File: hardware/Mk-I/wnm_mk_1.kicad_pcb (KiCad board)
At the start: 2 copper layers, 96.5 x 67.1 mm, 126 parts, among them CON1 USB-MICRO-B, SW1 SW_PUSH, SW10 SW_PUSH, SW11 SW_PUSH, SW12 SW_PUSH, SW13 SW_PUSH, SW14 SW_PUSH, SW15 SW_PUSH, SW16 SW_PUSH, SW18 SW_PUSH, SW19 SW_PUSH, SW2 SW_PUSH, SW20 SW_PUSH, SW21 SW_PUSH, SW22 SW_PUSH, SW3 SW_PUSH, SW4 SW_PUSH, SW5 SW_PUSH, SW6 SW_PUSH, SW7 SW_PUSH, SW8 SW_PUSH, SW9 SW_PUSH, U1 AP7313-18-SR-G-7, U10 STM32_SWD_Connector, U2 MCP73831, U3 BD33IA5, U4 STM32F407VG, U5 SGTL5000, U6 encoder_and_switch, U7 encoder_and_switch, U8 MOLEX_microSD_47219-2001, U9 SSD1306, X1 CRYSTAL

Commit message: HW: Update parts value
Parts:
- BAT1, D1, D10, D11, D12, D13, D14, D15, D16, D17, D2, D25, D3, D4, D5, D6, D7, D8, D9: value LED -> 150060RS75000
- CON1: value USB-MICRO-B -> 10118194-0001LF
- D18, D20, D21, D22, D23, D24: value LED -> 150060GS75000
- D27: value DOUBLE_SCH_KCOM_PMEG2005CT -> PMEG2005CT
- HP_OUT1, LINE_IN1: value 3.5_audio_jack -> lumberg 1503 02
- Play1, Play2, SW1, SW10, SW11, SW12, SW13, SW14, SW15, SW16, SW18, SW19, SW2, SW20, SW21, SW22, SW3, SW4, SW5, SW6, SW7, SW8, SW9, Write1: value SW_PUSH -> EVQ-Q2S02W
- U1: value AP7313-18-SR-G-7 -> AP7313-18SRG-7
- U2: value MCP73831 -> MCP73831T-2ACI/OT
- U3: value BD33IA5 -> BD33IA5MEFJ-ME2
- U4: value STM32F407VG -> STM32F427VIT6
- U5: value SGTL5000 -> SGTL5000XNAA3R2
- U6, U7: value encoder_and_switch -> EC12D1524403
- U8: value MOLEX_microSD_47219-2001 -> 47219-2001
- X1: value CRYSTAL -> AS-8.000-18

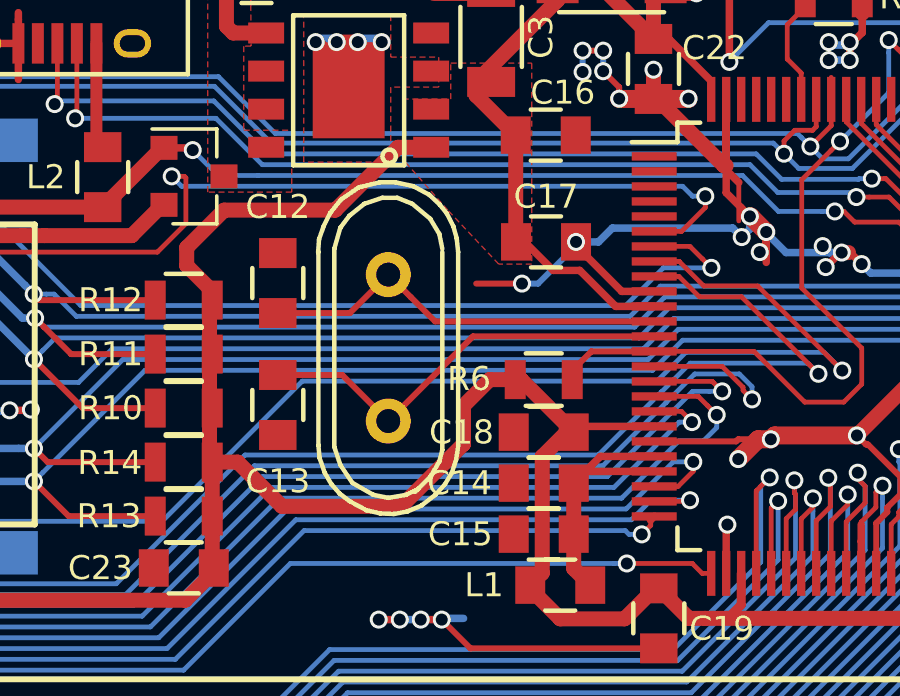
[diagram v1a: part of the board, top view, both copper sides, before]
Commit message: HW: Change crystal for a smd package
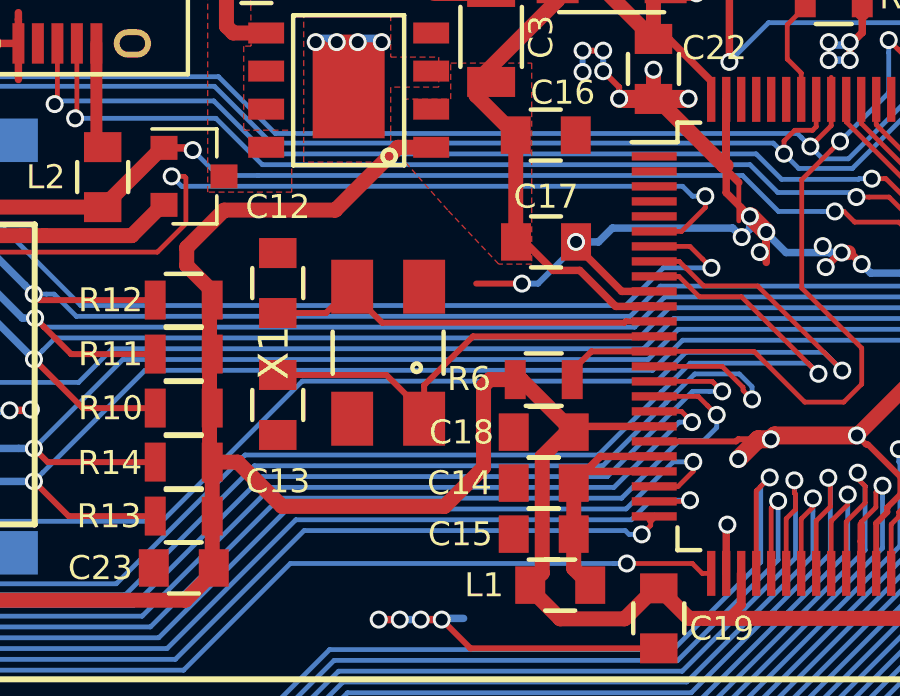
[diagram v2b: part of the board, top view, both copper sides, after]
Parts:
- HP_OUT1, LINE_IN1: value lumberg 1503 02 -> 1503 02
- X1: value AS-8.000-18 -> ABM3B-8.000MHZ-B2-T; footprint Crystals:Crystal_HC49-U_Vertical -> Crystals:Crystal_SMD_0603_4Pads
- moved X1 0.16 mm to (139.3, 93.3), turned to 90 degrees
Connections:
- X1 pad 1: Net-(C12-Pad2) -> Net-(C13-Pad2)
- X1 pad 2: Net-(C13-Pad2) -> GND
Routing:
- net 3V3: track 240.4 -> 241.2 mm
- net Net-(C13-Pad2): track 14.4 -> 15.1 mm

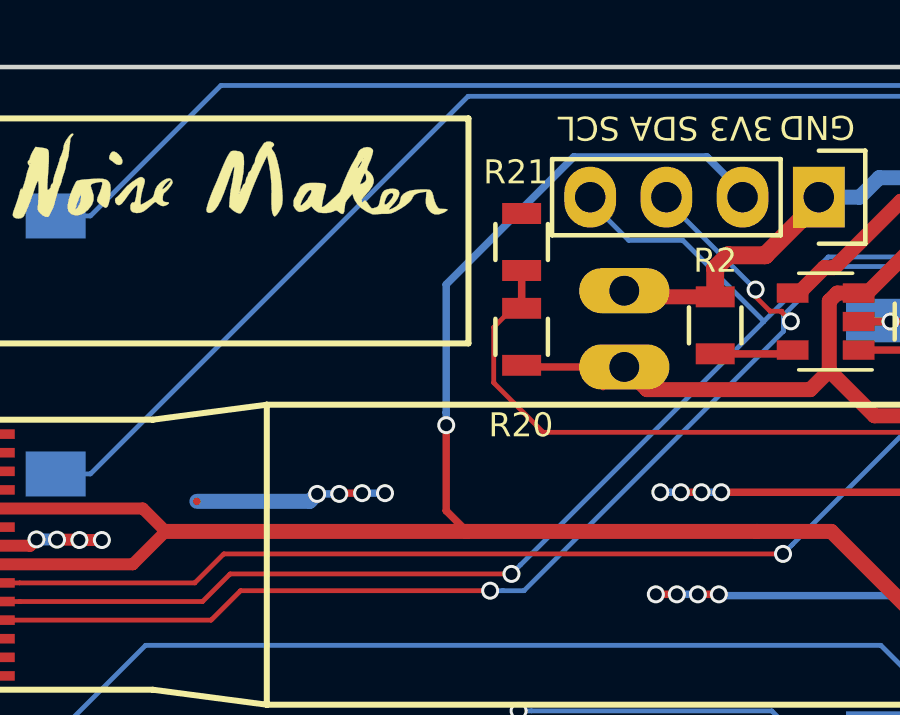
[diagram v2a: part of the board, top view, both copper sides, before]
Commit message: HW: Change battery connector to SMD
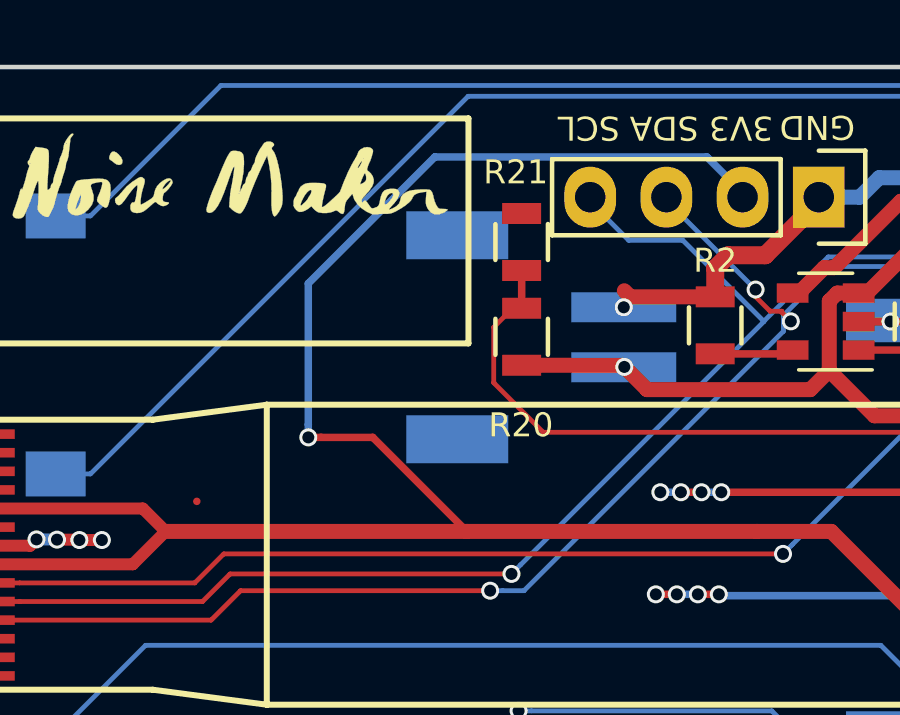
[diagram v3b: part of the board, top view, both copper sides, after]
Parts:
- BT1: value BATTERY -> S2B-PH-SM4-TB; footprint Connect:PINHEAD1-2 -> Connectors_JST:JST_PH_S2B-PH-SM4-TB_02x2.00mm_Angled
- moved BT1 2.81 mm to (107.2, 86.7)
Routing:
- net 3V3: track 241.2 -> 249.0 mm
- net (no net): track 6.39 -> 0.00 mm, vias 4 -> 0
- net VBAT: track 34.8 -> 33.8 mm, vias 0 -> 1
- net GND: track 217.0 -> 216.2 mm, vias 86 -> 87

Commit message: HW: Major change of layout...
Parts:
- removed D20, D21, D22, D23, D24: 150060GS75000, LEDs:LED_0805
- removed D25: 150060RS75000, LEDs:LED_0805
- removed REF**: MountingHole_4.3mm_M4, Mounting_Holes:MountingHole_4.3mm_M4
- removed SW18, SW19: EVQ-Q2S02W, Buttons_Switches_SMD:SW_SPST_B3SL-1002P
- removed ext1: CONN_01X04, Socket_Strips:Socket_Strip_Straight_1x04
- R9: value 330 -> 10K
- moved SW21 72.0 mm to (77.5, 123.2)
- moved SW20 65.1 mm to (77.5, 134.6)
- moved U9 29.4 mm to (111.8, 114.8)
- moved C25 29.3 mm to (109.0, 109.7)
- moved C27 29.3 mm to (109.0, 115.0)
- moved C28 29.3 mm to (109.0, 105.9)
- moved R15 29.3 mm to (109.0, 111.5)
- moved C29 29.3 mm to (109.0, 107.9)
- moved C26 29.3 mm to (109.0, 113.2)
- moved R9 24.3 mm to (182.2, 119.5), turned to 0 degrees
- moved LINE_IN1 10.6 mm to (72.0, 94.2)
- moved U6 10.2 mm to (78.7, 109.0)
- moved C30 10.2 mm to (74.1, 100.3)
- moved C31 10.2 mm to (83.3, 100.3)
- moved C32 10.2 mm to (90.2, 100.3)
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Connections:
- Play1 pad 1: Play -> 3V3
- Play1 pad 2: WAKEUP -> Play_WKUP
- Play2 pad 1: FX -> BUTTON_COL11
- Play2 pad 2: WAKEUP -> BUTTON_ROW2
- R9 pad 1: ROW3 -> GND
- R9 pad 2: Net-(D20-Pad2) -> Play_WKUP
- SW1 pad 1: B1 -> BUTTON_COL2
- SW1 pad 2: WAKEUP -> BUTTON_ROW1
- SW10 pad 1: B10 -> BUTTON_COL3
- SW10 pad 2: WAKEUP -> BUTTON_ROW2
- SW11 pad 1: B11 -> BUTTON_COL4
- SW11 pad 2: WAKEUP -> BUTTON_ROW2
- SW12 pad 1: B12 -> BUTTON_COL5
- SW12 pad 2: WAKEUP -> BUTTON_ROW2
- SW13 pad 1: B13 -> BUTTON_COL6
- SW13 pad 2: WAKEUP -> BUTTON_ROW2
- SW14 pad 1: B14 -> BUTTON_COL7
- SW14 pad 2: WAKEUP -> BUTTON_ROW2
- SW15 pad 1: B15 -> BUTTON_COL8
- SW15 pad 2: WAKEUP -> BUTTON_ROW2
- SW16 pad 1: B16 -> BUTTON_COL9
- SW16 pad 2: WAKEUP -> BUTTON_ROW2
- SW2 pad 1: B2 -> BUTTON_COL3
- SW2 pad 2: WAKEUP -> BUTTON_ROW1
- SW20 pad 1: BC -> BUTTON_COL1
- SW20 pad 2: WAKEUP -> BUTTON_ROW2
- SW21 pad 1: BD -> BUTTON_COL1
- SW21 pad 2: WAKEUP -> BUTTON_ROW1
- SW22 pad 1: BE -> BUTTON_COL10
- SW22 pad 2: WAKEUP -> BUTTON_ROW1
- SW3 pad 1: B3 -> BUTTON_COL4
- SW3 pad 2: WAKEUP -> BUTTON_ROW1
- SW4 pad 1: B4 -> BUTTON_COL5
- SW4 pad 2: WAKEUP -> BUTTON_ROW1
- SW5 pad 1: B5 -> BUTTON_COL6
- SW5 pad 2: WAKEUP -> BUTTON_ROW1
- SW6 pad 1: B6 -> BUTTON_COL7
- SW6 pad 2: WAKEUP -> BUTTON_ROW1
- SW7 pad 1: B7 -> BUTTON_COL8
- SW7 pad 2: WAKEUP -> BUTTON_ROW1
- SW8 pad 1: B8 -> BUTTON_COL9
- SW8 pad 2: WAKEUP -> BUTTON_ROW1
- SW9 pad 1: B9 -> BUTTON_COL2
- SW9 pad 2: WAKEUP -> BUTTON_ROW2
- U4 pad 16: B1 -> Net-(U4-Pad16)
- U4 pad 18: B9 -> Net-(U4-Pad18)
- U4 pad 23: WAKEUP -> PLAY_WAKEUP
- U4 pad 25: B2 -> Net-(U4-Pad25)
- U4 pad 33: B3 -> Net-(U4-Pad33)
- U4 pad 34: B11 -> Net-(U4-Pad34)
- U4 pad 36: BA -> Net-(U4-Pad36)
- U4 pad 38: B4 -> Net-(U4-Pad38)
- U4 pad 39: B12 -> Net-(U4-Pad39)
- U4 pad 41: BB -> Net-(U4-Pad41)
- U4 pad 42: B5 -> Net-(U4-Pad42)
- U4 pad 43: B13 -> Net-(U4-Pad43)
- U4 pad 45: BC -> Net-(U4-Pad45)
- U4 pad 46: B6 -> Net-(U4-Pad46)
- U4 pad 47: B14 -> Net-(U4-Pad47)
- U4 pad 51: B15 -> Net-(U4-Pad51)
- U4 pad 52: B7 -> Net-(U4-Pad52)
- U4 pad 53: BD -> Net-(U4-Pad53)
- U4 pad 55: BE -> Net-(U4-Pad55)
- U4 pad 56: B8 -> Net-(U4-Pad56)
- U4 pad 57: B16 -> Net-(U4-Pad57)
- U4 pad 58: ROW3 -> Net-(U4-Pad58)
- U4 pad 62: FX -> Net-(U4-Pad62)
- U4 pad 63: Play -> Net-(U4-Pad63)
- U6 pad 4: WAKEUP -> BUTTON_COL1
- U6 pad 5: ENC_1_SW -> BUTTON_ROW3
- U7 pad 4: WAKEUP -> BUTTON_COL3
- U7 pad 5: ENC_2_SW -> BUTTON_ROW3
- Write1 pad 1: Write -> BUTTON_COL10
- Write1 pad 2: WAKEUP -> BUTTON_ROW2
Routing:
- net WAKEUP: track 348.3 -> 0.00 mm, vias 1 -> 0
- net BUTTON_ROW2: track 0.00 -> 129.8 mm, vias 0 -> 2
- net BUTTON_ROW1: track 0.00 -> 104.2 mm, vias 0 -> 2
- net B9: track 101.4 -> 0.00 mm, vias 2 -> 0
- net B1: track 93.1 -> 0.00 mm, vias 2 -> 0
- net B10: track 86.3 -> 0.00 mm, vias 2 -> 0
- net COL1: track 98.4 -> 14.0 mm, vias 3 -> 2
- net B11: track 82.3 -> 0.00 mm, vias 2 -> 0
- net B12: track 80.9 -> 0.00 mm, vias 2 -> 0
- net ENC_1_SW: track 78.9 -> 0.00 mm, vias 1 -> 0
- net COL2: track 92.3 -> 14.2 mm, vias 3 -> 2
- net B2: track 75.5 -> 0.00 mm, vias 2 -> 0
- net B3: track 72.2 -> 0.00 mm, vias 2 -> 0
- net B13: track 70.8 -> 0.00 mm, vias 2 -> 0
- net ENC_1_A: track 79.9 -> 9.21 mm, vias 2 -> 1
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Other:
- board size 96.5 x 67.1 mm -> 106.7 x 67.1 mm
- board text added: "MENU"
- board text added: "PATTERN"
- board text added: "SHIFT"
- board text added: "TRACK"
- board text removed: "3V3"
- board text removed: "A"
- board text removed: "B"
- board text removed: "C"
- board text removed: "D"
- board text removed: "E"
- board text removed: "FX"
- board text removed: "SCL"
- board text removed: "SDA"

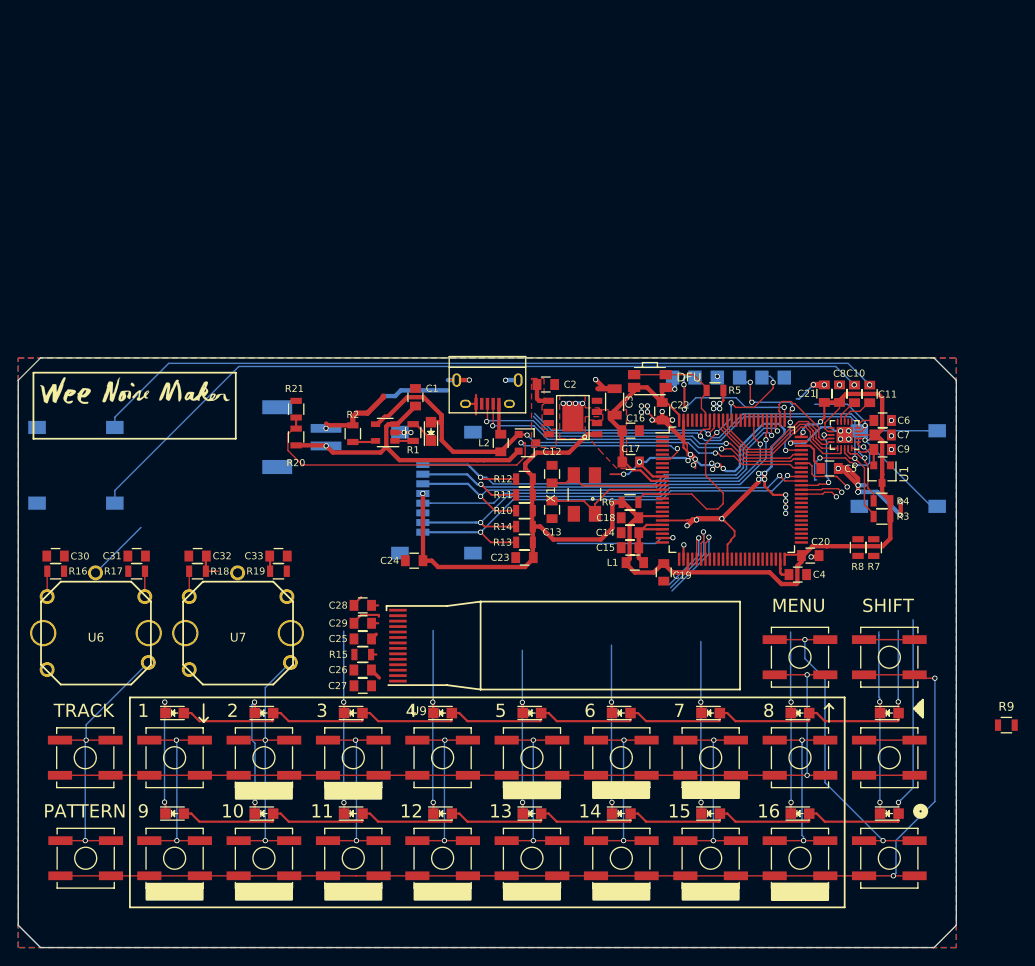
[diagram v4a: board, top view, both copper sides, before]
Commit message: HW: Change micro SD card slot
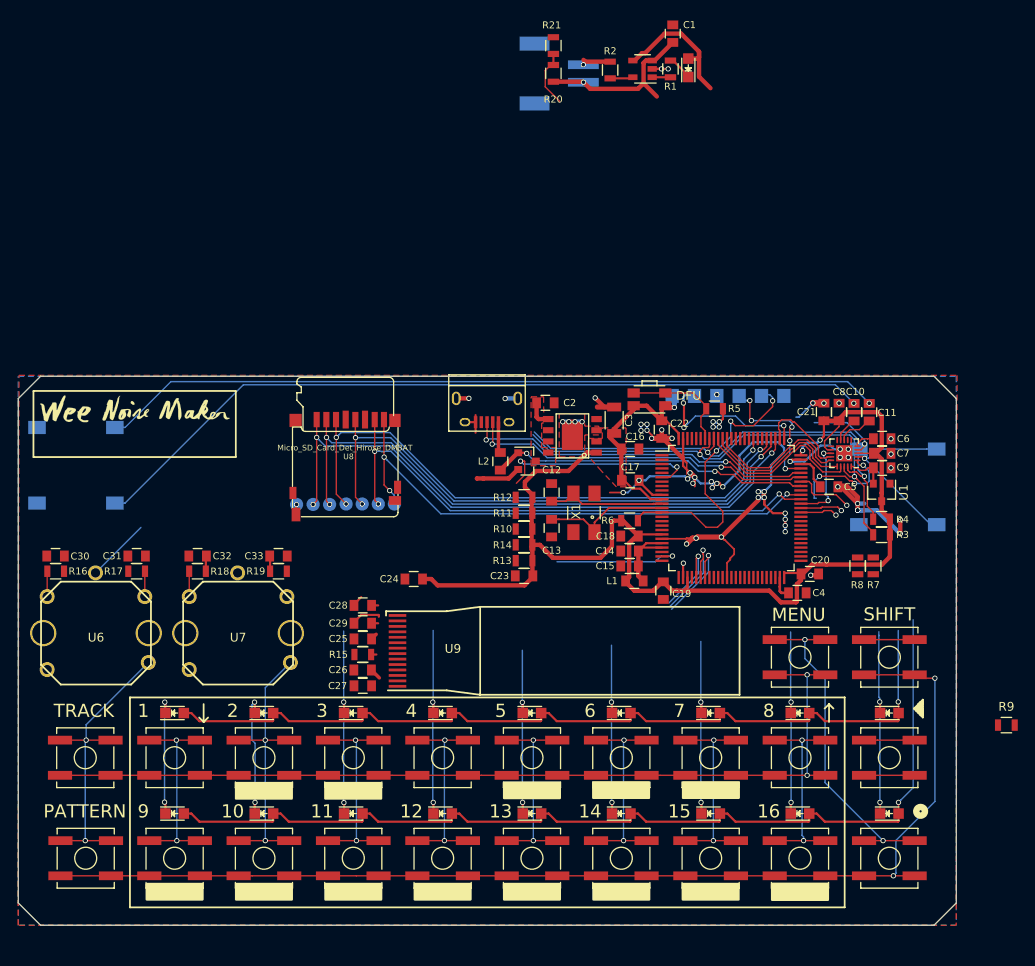
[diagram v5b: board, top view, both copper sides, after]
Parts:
- added TP_CLK1: TEST, Measurement_Points:Measurement_Point_Round-SMD-Pad_Small, B.Cu at (109.0, 94.3)
- added TP_CMD1: TEST, Measurement_Points:Measurement_Point_Round-SMD-Pad_Small, B.Cu at (107.1, 94.3)
- added TP_DAT0: TEST, Measurement_Points:Measurement_Point_Round-SMD-Pad_Small, B.Cu at (110.8, 94.3)
- added TP_DAT1: TEST, Measurement_Points:Measurement_Point_Round-SMD-Pad_Small, B.Cu at (112.6, 94.3)
- added TP_DAT2: TEST, Measurement_Points:Measurement_Point_Round-SMD-Pad_Small, B.Cu at (103.4, 94.4)
- added TP_DAT3: TEST, Measurement_Points:Measurement_Point_Round-SMD-Pad_Small, B.Cu at (105.3, 94.4)
- added TP_DETECT0: TEST, Measurement_Points:Measurement_Point_Round-SMD-Pad_Small, B.Cu at (101.5, 94.4)
- U8: value 47219-2001 -> Micro_SD_Card_Det_Hirose_DM3AT; footprint POSS:MOLEX_microSD_47219-2001 -> POSS:DM3D; moved to F.Cu
- moved BAT1 50.7 mm to (146.1, 44.7)
- moved R21 50.7 mm to (130.7, 42.2)
- moved C1 50.7 mm to (144.3, 40.8)
- moved R1 50.7 mm to (144.0, 44.9)
- moved R20 50.7 mm to (130.7, 45.4)
- moved BT1 50.7 mm to (131.3, 45.4)
- moved R2 50.7 mm to (137.2, 45.0)
- moved U2 50.7 mm to (140.8, 44.9)
- moved U8 15.6 mm to (113.0, 84.3), turned to 180 degrees
- moved C13 2.08 mm to (130.5, 97.1)
- moved C14 2.08 mm to (139.4, 99.7)
- moved C16 2.08 mm to (139.4, 88.1)
- moved C4 2.08 mm to (158.4, 104.4)
- moved C5 2.08 mm to (162.1, 92.4)
- moved C6 2.08 mm to (168.1, 86.9)
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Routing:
- net VBAT_SENSE: track 54.8 -> 30.5 mm
- net SD_DAT2: track 50.7 -> 70.0 mm, vias 2 -> 3
- net SD_CLK: track 45.5 -> 64.3 mm, vias 1 -> 3
- net SD_DAT3: track 50.5 -> 68.1 mm, vias 2 -> 3
- net GND: track 156.9 -> 141.3 mm
- net SD_CMD: track 50.4 -> 65.6 mm, vias 2 -> 3
- net SD_DAT0: track 49.7 -> 62.1 mm, vias 2 -> 3
- net SD_DAT1: track 50.3 -> 61.1 mm, vias 2 -> 3
- net VBAT: track 33.8 -> 25.0 mm
- net 3V3: track 180.1 -> 172.4 mm, vias 4 -> 3
- net VBUS: track 58.7 -> 53.3 mm
- net Net-(C10-Pad1): track 92.3 -> 90.5 mm
- net Net-(C11-Pad1): track 90.6 -> 89.0 mm
- net ENC_2_A: track 14.4 -> 12.9 mm
- net SD_DETECT: track 0.00 -> 1.17 mm, vias 0 -> 1
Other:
- board size 106.7 x 67.1 mm -> 106.7 x 62.4 mm
- board text added: "CLK"
- board text added: "CMD"
- board text added: "DAT0"
- board text added: "DAT1"
- board text added: "DAT2"
- board text added: "DAT3"
- board text added: "DETECT"
- board text added: "Rev-D"
- board text removed: "Rev-C"

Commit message: HW: Use folded foot print for the OLED screen
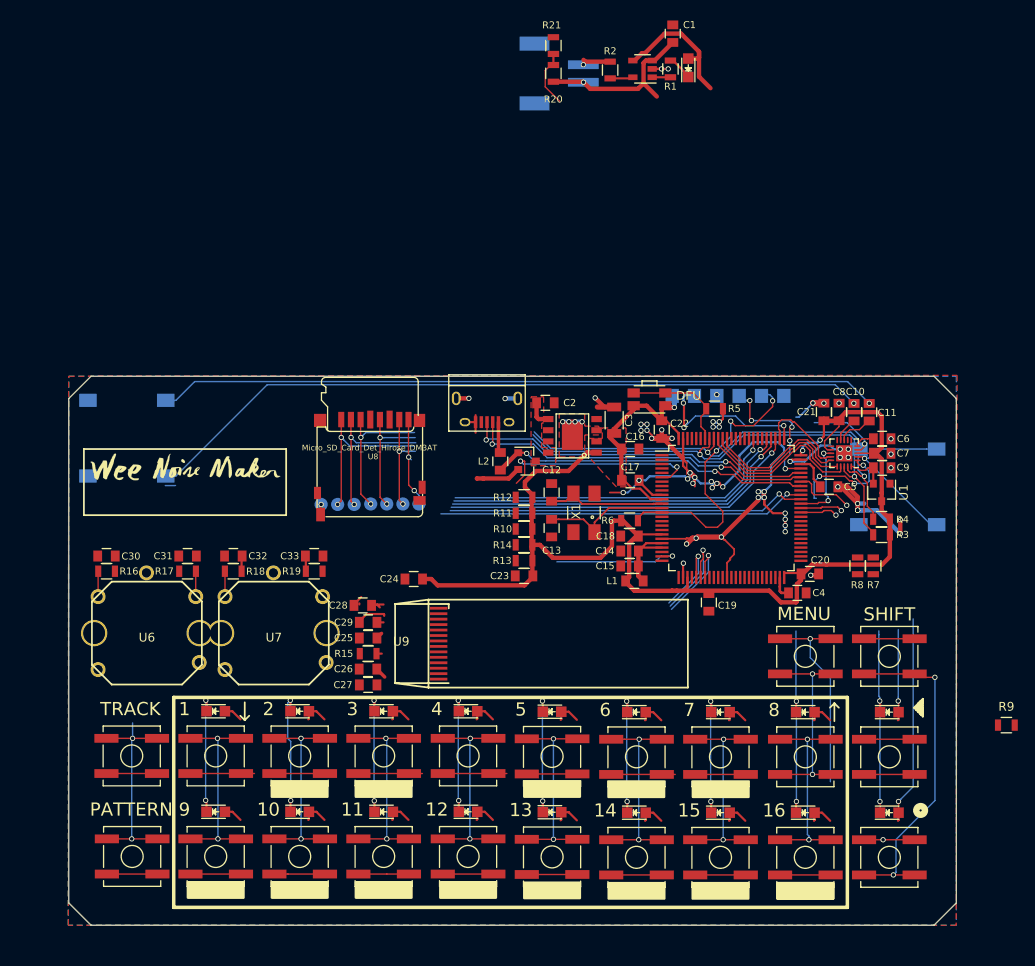
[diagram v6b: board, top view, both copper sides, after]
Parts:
- U9: footprint POSS:MIDAS_MCOT096016AV_OLED -> POSS:MIDAS_MCOT096016AV_OLED_FOLDED
- moved G*** 8.75 mm to (88.8, 93.6)
- moved G*** 8.75 mm to (88.8, 90.1)
- moved LINE_IN1 6.56 mm to (77.8, 91.2)
- moved U9 5.93 mm to (105.9, 114.6)
- moved C31 5.79 mm to (89.1, 100.3)
- moved R16 5.79 mm to (79.9, 102.0)
- moved R17 5.79 mm to (89.1, 102.0)
- moved U6 5.79 mm to (84.5, 109.0)
- moved C30 5.79 mm to (79.9, 100.3)
- moved C19 5.35 mm to (148.4, 105.5)
- moved SW20 5.29 mm to (82.8, 134.4)
- moved SW21 5.29 mm to (82.8, 123.0)
- moved SW9 4.68 mm to (92.3, 134.4)
- moved D10 4.68 mm to (92.3, 117.9)
- moved SW1 4.68 mm to (92.3, 123.0)
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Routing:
- net Net-(D1-Pad2): track 114.1 -> 47.6 mm
- net Net-(D10-Pad2): track 100.8 -> 34.3 mm
- net BUTTON_ROW2: track 129.8 -> 90.1 mm
- net BUTTON_ROW1: track 104.2 -> 75.1 mm
- net SD_CMD: track 65.6 -> 55.2 mm
- net SD_CLK: track 64.3 -> 54.1 mm
- net BUTTON_COL3: track 32.9 -> 22.9 mm
- net BUTTON_COL1: track 34.7 -> 24.7 mm
- net SD_DAT3: track 68.1 -> 58.2 mm
- net SD_DAT2: track 70.0 -> 60.1 mm
- net SD_DAT0: track 62.1 -> 52.5 mm
- net BUTTON_COL10: track 38.0 -> 28.7 mm
- net SD_DAT1: track 61.1 -> 52.4 mm
- net COL4: track 22.1 -> 14.0 mm
- net COL3: track 22.1 -> 14.0 mm
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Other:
- board size 106.7 x 62.4 mm -> 100.9 x 62.4 mm
